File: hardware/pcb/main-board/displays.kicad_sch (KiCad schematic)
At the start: 1 part, among them J601 DISP_PCB x40 FPC

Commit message: make a start on RP2040 to replace the KB pico
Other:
- title: Z88R - Z88 Recreated -> Z88R - Z88 Recreation
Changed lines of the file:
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@@
 	(paper "A4")
 	(title_block
-		(title "Z88R - Z88 Recreated")
-		(date "2025-12-19")
-		(rev "20251219WIP")
+		(title "Z88R - Z88 Recreation")
+		(date "2025-12-30")
+		(rev "20251230WIP")
 		(company "Fountain and Menadue")
 	)

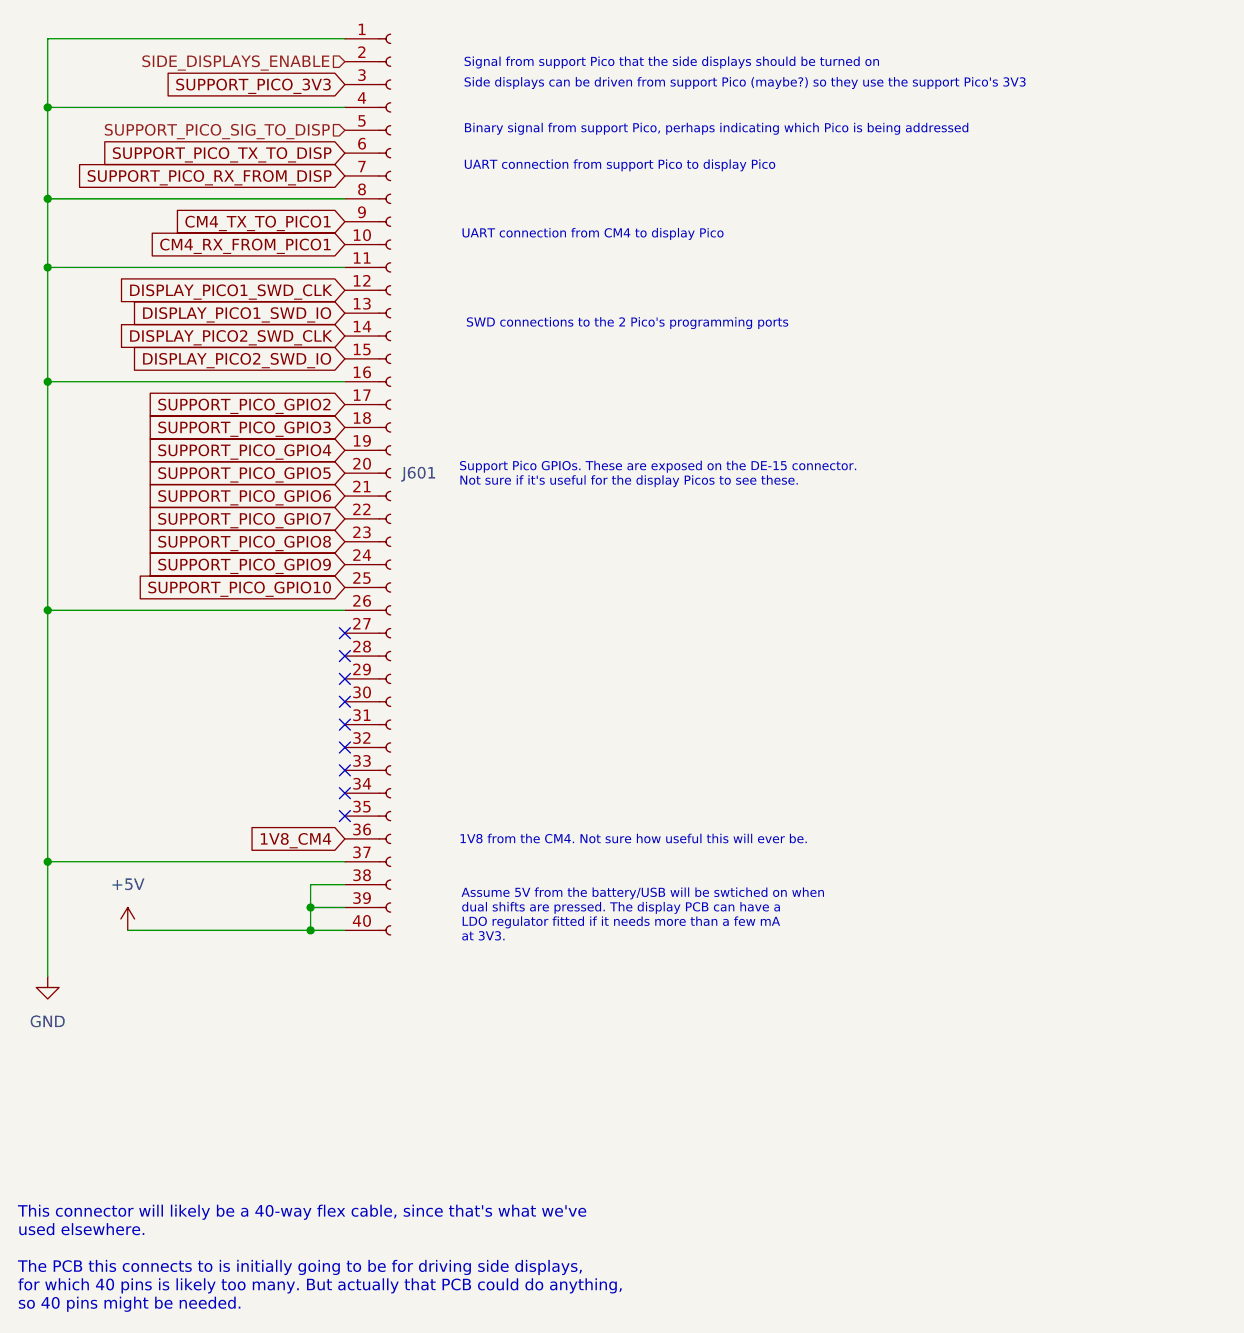
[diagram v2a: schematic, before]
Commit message: start the support pico rp2040 replacement
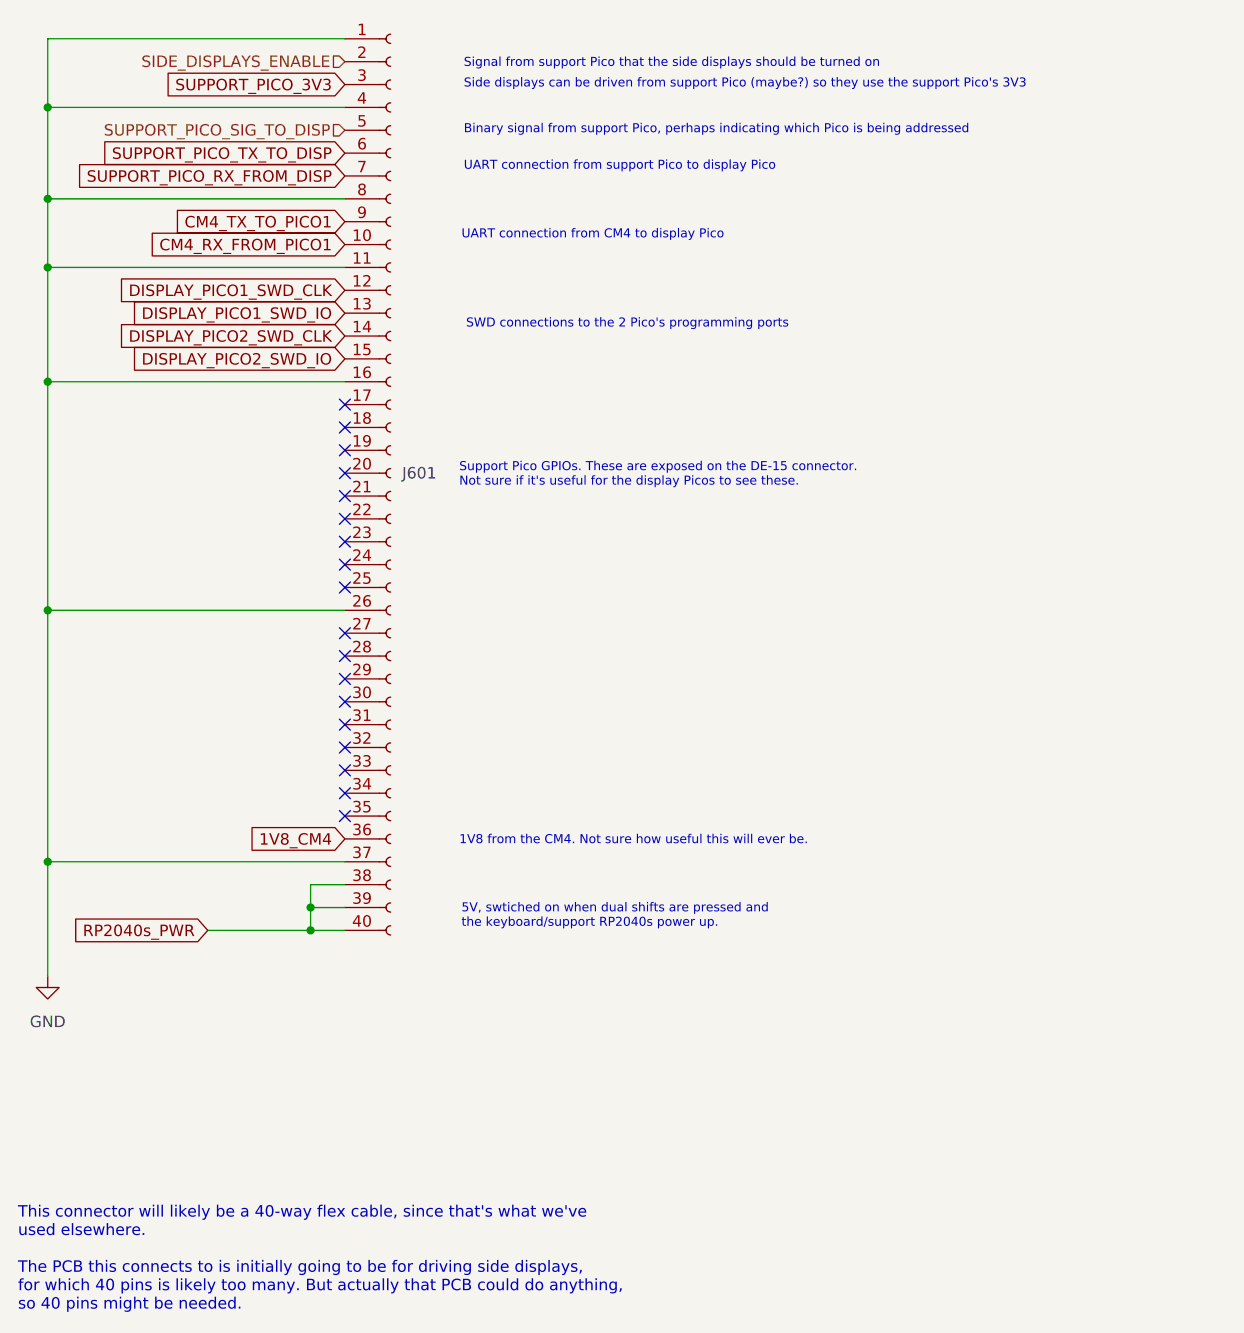
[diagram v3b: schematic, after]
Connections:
- net +5V renamed RP2040s_PWR
- net SUPPORT_PICO_GPIO10: no longer names the net of J601.25 (Pin_25)
- net SUPPORT_PICO_GPIO2: no longer names the net of J601.17 (Pin_17)
- net SUPPORT_PICO_GPIO3: no longer names the net of J601.18 (Pin_18)
- net SUPPORT_PICO_GPIO4: no longer names the net of J601.19 (Pin_19)
- net SUPPORT_PICO_GPIO5: no longer names the net of J601.20 (Pin_20)
- net SUPPORT_PICO_GPIO6: no longer names the net of J601.21 (Pin_21)
- net SUPPORT_PICO_GPIO7: no longer names the net of J601.22 (Pin_22)
- net SUPPORT_PICO_GPIO8: no longer names the net of J601.23 (Pin_23)
- net SUPPORT_PICO_GPIO9: no longer names the net of J601.24 (Pin_24)
- no-connect marks 9 -> 18
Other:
- note added: "5V, swtiched on when dual shifts are pressed and the keyboard/support RP2040s power up."
- note removed: "Assume 5V from the battery/USB will be swtiched on when dual shifts are pressed. The display PCB can have a LDO regulator fitted if it needs more than a few mA at 3V3."

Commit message: rename the pico bits to RP2040, still a few things to check
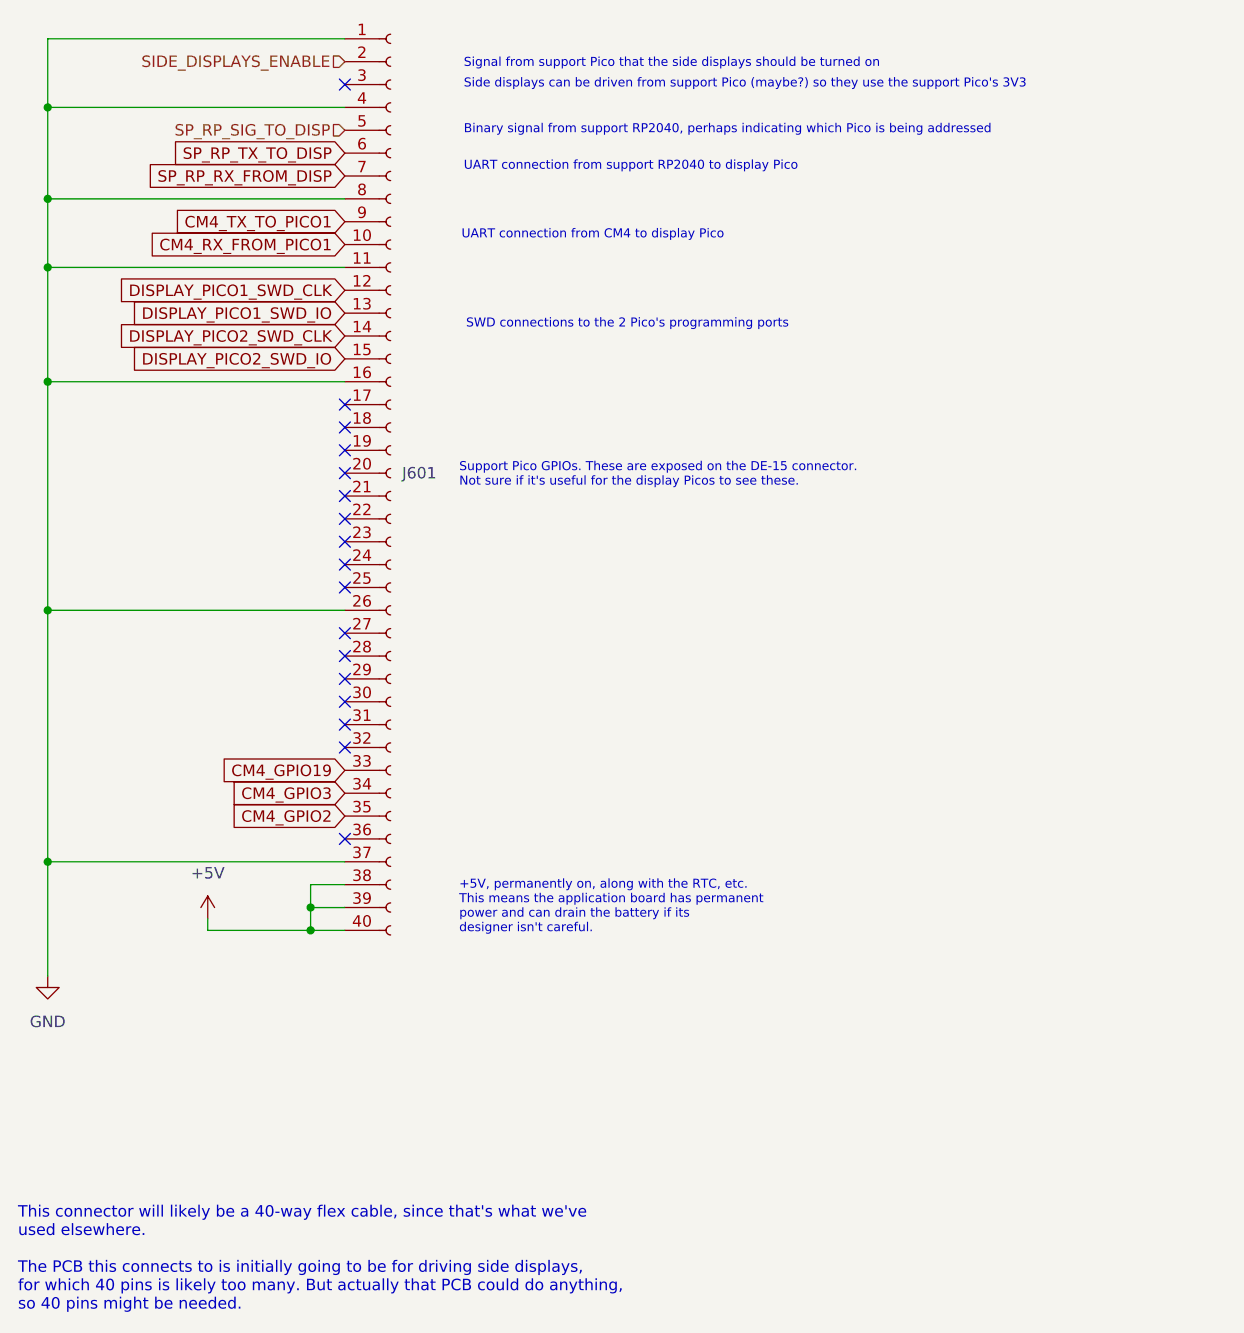
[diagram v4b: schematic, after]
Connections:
- net CM4_GPIO19: now reaches J601.33 (Pin_33)
- net CM4_GPIO3: now reaches J601.34 (Pin_34)
- net CM4_GPIO2: now reaches J601.35 (Pin_35)
- net 1V8_CM4: no longer names the net of J601.36 (Pin_36)
- net RP2040s_PWR renamed +5V
- net SUPPORT_PICO_3V3: no longer names the net of J601.3 (Pin_3)
- net SUPPORT_PICO_RX_FROM_DISP renamed SP_RP_RX_FROM_DISP
- net SUPPORT_PICO_SIG_TO_DISP renamed SP_RP_SIG_TO_DISP
- net SUPPORT_PICO_TX_TO_DISP renamed SP_RP_TX_TO_DISP
- no-connect marks 18 -> 17
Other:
- note added: "+5V, permanently on, along with the RTC, etc. This means the application board has permanent power and can drain the battery if its designer isn't careful."
- note added: "Binary signal from support RP2040, perhaps indicating which Pico is being addressed"
- note added: "UART connection from support RP2040 to display Pico"
- note removed: "1V8 from the CM4. Not sure how useful this will ever be."
- note removed: "5V, swtiched on when dual shifts are pressed and the keyboard/support RP2040s power up."
- note removed: "Binary signal from support Pico, perhaps indicating which Pico is being addressed"
- note removed: "UART connection from support Pico to display Pico"
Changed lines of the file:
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@@
 	)
 	(no_connect
-		(at 58.42 104.14)
+		(at 58.42 27.94)
 	)
 	(no_connect
@@
 	)
 	(no_connect
-		(at 58.42 106.68)
-	)
-	(no_connect
 		(at 58.42 93.98)
 	)
 	(no_connect
+		(at 58.42 111.76)
+	)
+	(no_connect
 		(at 58.42 68.58)
 	)
@@
 	)
 	(no_connect
-		(at 58.42 109.22)
-	)
-	(no_connect
 		(at 58.42 63.5)
 	)
@@
 	(wire
 		(pts
+			(xy 43.18 120.65) (xy 43.18 121.92)
+		)
+		(stroke
+			(width 0)
+			(type default)
+		)
+	)
+	(wire
+		(pts
 			(xy 43.18 121.92) (xy 54.61 121.92)
 		)
@@
 		)
 	)
-	(text "1V8 from the CM4. Not sure how useful this will ever be."
-		(exclude_from_sim no)
-		(at 71.12 112.014 0)
-		(effects
-			(font
-				(size 1 1)
-			)
-			(justify left)
-		)
-	)
-	(text "5V, swtiched on when dual shifts are pressed and\nthe keyboard/support RP2040s power up."
-		(exclude_from_sim no)
-		(at 71.374 120.396 0)
+	(text "+5V, permanently on, along with the RTC, etc.\nThis means the application board has permanent\npower and can drain the battery if its\ndesigner isn't careful."
+		(exclude_from_sim no)
+		(at 71.12 119.38 0)
 		(effects
 			(font
@@
 		)
 	)
-	(text "UART connection from support Pico to display Pico"
+	(text "UART connection from support RP2040 to display Pico"
 		(exclude_from_sim no)
 		(at 71.628 37.084 0)
@@
 		)
 	)
-	(text "Binary signal from support Pico, perhaps indicating which Pico is being addressed"
+	(text "Binary signal from support RP2040, perhaps indicating which Pico is being addressed"
 		(exclude_from_sim no)
 		(at 71.628 33.02 0)
@@
 		)
 	)
+	(global_label "CM4_GPIO19"
+		(shape input)
+		(at 58.42 104.14 180)
+		(fields_autoplaced yes)
+		(effects
+			(font
+				(size 1.27 1.27)
+			)
+			(justify right)
+		)
+		(property "Intersheetrefs" "${INTERSHEET_REFS}"
+			(at 44.2962 104.14 0)
+			(effects
+				(font
+					(size 1.27 1.27)
+				)
+				(justify right)
+				(hide yes)
+			)
+		)
+	)
 	(global_label "DISPLAY_PICO1_SWD_CLK"
 		(shape input)
@@
 		)
 	)
+	(global_label "SP_RP_TX_TO_DISP"
+		(shape input)
+		(at 58.42 35.56 180)
+		(fields_autoplaced yes)
+		(effects
+			(font
+				(size 1.27 1.27)
+			)
+			(justify right)
+		)
+		(property "Intersheetrefs" "${INTERSHEET_REFS}"
+			(at 38.3696 35.56 0)
+			(effects
+				(font
+					(size 1.27 1.27)
+				)
+				(justify right)
+				(hide yes)
+			)
+		)
+	)
 	(global_label "CM4_RX_FROM_PICO1"
 		(shape input)
@@
 		)
 	)
-	(global_label "RP2040s_PWR"
-		(shape input)
-		(at 43.18 121.92 180)
-		(fields_autoplaced yes)
-		(effects
-			(font
-				(size 1.27 1.27)
-			)
-			(justify right)
-		)
-		(property "Intersheetrefs" "${INTERSHEET_REFS}"
-			(at 27.4839 121.92 0)
-			(effects
-				(font
-					(size 1.27 1.27)
-				)
-				(justify right)
-				(hide yes)
-			)
-		)
-	)
-	(global_label "SUPPORT_PICO_TX_TO_DISP"
-		(shape input)
-		(at 58.42 35.56 180)
-		(fields_autoplaced yes)
-		(effects
-			(font
-				(size 1.27 1.27)
-			)
-			(justify right)
-		)
-		(property "Intersheetrefs" "${INTERSHEET_REFS}"
-			(at 30.2657 35.56 0)
+	(global_label "CM4_GPIO3"
+		(shape input)
+		(at 58.42 106.68 180)
+		(fields_autoplaced yes)
+		(effects
+			(font
+				(size 1.27 1.27)
+			)
+			(justify right)
+		)
+		(property "Intersheetrefs" "${INTERSHEET_REFS}"
+			(at 45.5057 106.68 0)
+			(effects
+				(font
+					(size 1.27 1.27)
+				)
+				(justify right)
+				(hide yes)
+			)
+		)
+	)
+	(global_label "CM4_GPIO2"
+		(shape input)
+		(at 58.42 109.22 180)
+		(fields_autoplaced yes)
+		(effects
+			(font
+				(size 1.27 1.27)
+			)
+			(justify right)
+		)
+		(property "Intersheetrefs" "${INTERSHEET_REFS}"
+			(at 45.5057 109.22 0)
 			(effects
 				(font
@@
 		)
 	)
-	(global_label "1V8_CM4"
-		(shape input)
-		(at 58.42 111.76 180)
-		(fields_autoplaced yes)
-		(effects
-			(font
-				(size 1.27 1.27)
-			)
-			(justify right)
-		)
-		(property "Intersheetrefs" "${INTERSHEET_REFS}"
-			(at 47.6829 111.76 0)
-			(effects
-				(font
-					(size 1.27 1.27)
-				)
-				(justify right)
-				(hide yes)
-			)
-		)
-	)
-	(global_label "SUPPORT_PICO_3V3"
-		(shape input)
-		(at 58.42 27.94 180)
-		(fields_autoplaced yes)
-		(effects
-			(font
-				(size 1.27 1.27)
-			)
-			(justify right)
-		)
-		(property "Intersheetrefs" "${INTERSHEET_REFS}"
-			(at 37.5228 27.94 0)
-			(effects
-				(font
-					(size 1.27 1.27)
-				)
-				(justify right)
-				(hide yes)
-			)
-		)
-	)
-	(global_label "SUPPORT_PICO_RX_FROM_DISP"
+	(global_label "SP_RP_RX_FROM_DISP"
 		(shape input)
 		(at 58.42 38.1 180)
@@
 		)
 		(property "Intersheetrefs" "${INTERSHEET_REFS}"
-			(at 27.1209 38.1 0)
+			(at 35.2248 38.1 0)
 			(effects
 				(font
@@
 		)
 	)
-	(hierarchical_label "SUPPORT_PICO_SIG_TO_DISP"
+	(hierarchical_label "SP_RP_SIG_TO_DISP"
 		(shape input)
 		(at 58.42 33.02 180)
@@
 		)
 	)
+	(symbol
+		(lib_id "power:+5V")
+		(at 43.18 120.65 0)
+		(unit 1)
+		(exclude_from_sim no)
+		(in_bom yes)
+		(on_board yes)
+		(dnp no)
+		(fields_autoplaced yes)
+		(property "Reference" "#PWR602"
+			(at 43.18 124.46 0)
+			(effects
+				(font
+					(size 1.27 1.27)
+				)
+				(hide yes)
+			)
+		)
+		(property "Value" "+5V"
+			(at 43.18 115.57 0)
+			(effects
+				(font
+					(size 1.27 1.27)
+				)
+			)
+		)
+		(property "Footprint" ""
+			(at 43.18 120.65 0)
+			(effects
+				(font
+					(size 1.27 1.27)
+				)
+				(hide yes)
+			)
+		)
+		(property "Datasheet" ""
+			(at 43.18 120.65 0)
+			(effects
+				(font
+					(size 1.27 1.27)
+				)
+				(hide yes)
+			)
+		)
+		(property "Description" "Power symbol creates a global label with name \"+5V\""
+			(at 43.18 120.65 0)
+			(effects
+				(font
+					(size 1.27 1.27)
+				)
+				(hide yes)
+			)
+		)
+		(pin "1"
+		)
+		(instances
+			(project ""
+				(path "/fdce8012-5f35-4f58-8abb-80214b4af8fe/b021e735-62db-4e44-b9a4-83c0ced3ecfd"
+					(reference "#PWR602")
+					(unit 1)
+				)
+			)
+		)
+	)

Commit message: a few more tidyups, almost ready for dual shifts stuff now
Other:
- note removed: "Side displays can be driven from support Pico (maybe?) so they use the support Pico's 3V3"
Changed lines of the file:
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@@
-		)
-	)
-	(text "Side displays can be driven from support Pico (maybe?) so they use the support Pico's 3V3"
-		(exclude_from_sim no)
-		(at 71.628 27.94 0)
-		(effects
-			(font
-				(size 1 1)
-			)
-			(justify left)
 		)
 	)

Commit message: more support rp2040 cleanups
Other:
- note added: "Signal from support RP2040 that the side displays should be turned on"
- note removed: "Signal from support Pico that the side displays should be turned on"
- note removed: "Support Pico GPIOs. These are exposed on the DE-15 connector. Not sure if it's useful for the display Picos to see these."
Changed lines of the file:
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@@
 		)
 	)
-	(text "Signal from support Pico that the side displays should be turned on"
+	(text "Signal from support RP2040 that the side displays should be turned on"
 		(exclude_from_sim no)
 		(at 71.628 25.654 0)
@@
 		(effects
 			(font
-				(size 1 1)
-			)
-			(justify left)
-		)
-	)
-	(text "Support Pico GPIOs. These are exposed on the DE-15 connector.\nNot sure if it's useful for the display Picos to see these."
-		(exclude_from_sim no)
-		(at 71.12 71.374 0)
-		(effects
-			(font
